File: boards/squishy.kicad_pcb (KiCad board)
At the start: 4 copper layers, 82 x 76.8 mm, 217 parts, among them J1 USB_B_Micro, J2 Conn_02x26_Top_Bottom, J3 Conn_02x05_Odd_Even, U1 128MiB, U10 THVD1451, U11 THVD1451, U12 THVD1451, U13 THVD1451, U14 THVD1451, U15 THVD1451, U16 THVD1451, U17 THVD1451, U18 THVD1451, U19 THVD1451, U2 ICE40HX8K-BG121, U20 THVD1451, U21 TXB0106, U22 TXB0106, U23 TXB0106, U24 TXB0106, U25 TXB0106, U26 TXB0106, U27 FT240XQ, U28 MAX809JTRG, U29 TLV755533PDRVR, U3 THVD1451, U30 TLV73312PQDRVRQ1, U4 THVD1451, U5 THVD1451, U6 THVD1451, U7 THVD1451, U8 THVD1451, U9 THVD1451, X1 ASEM-48MHz

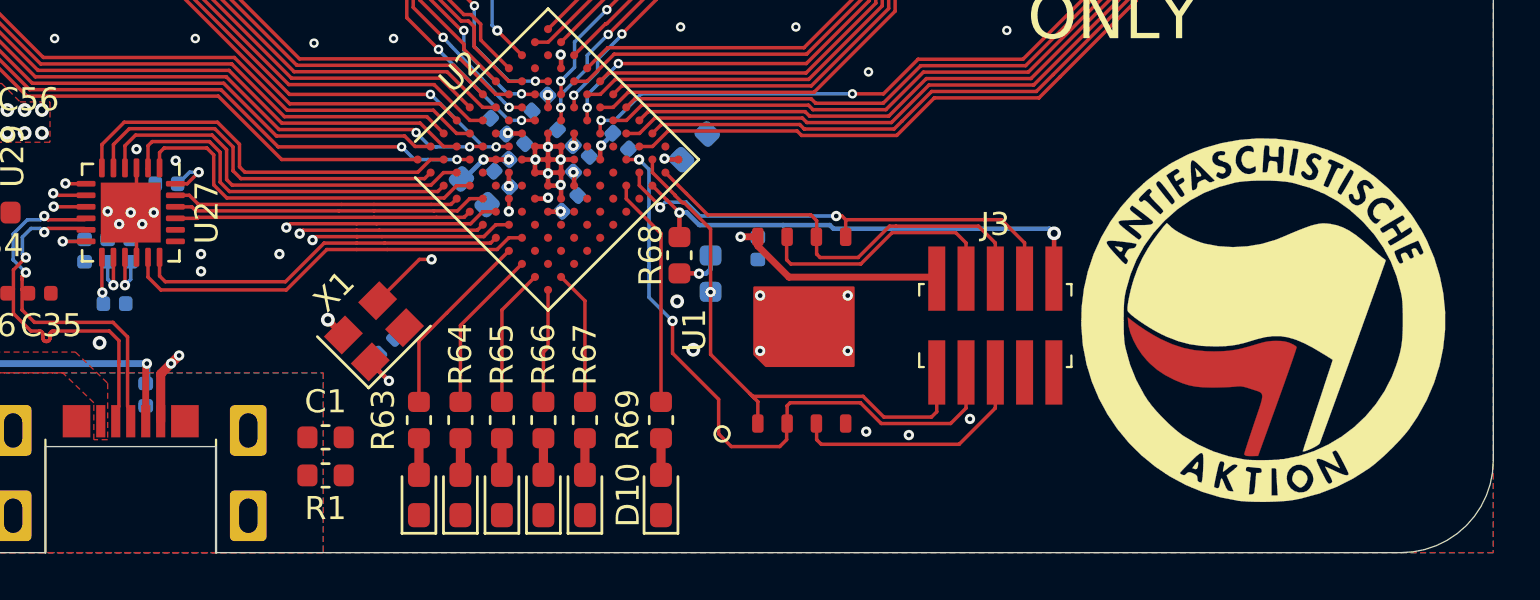
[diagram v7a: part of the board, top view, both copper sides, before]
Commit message: Moved some things around and cached the rev0 of squishy
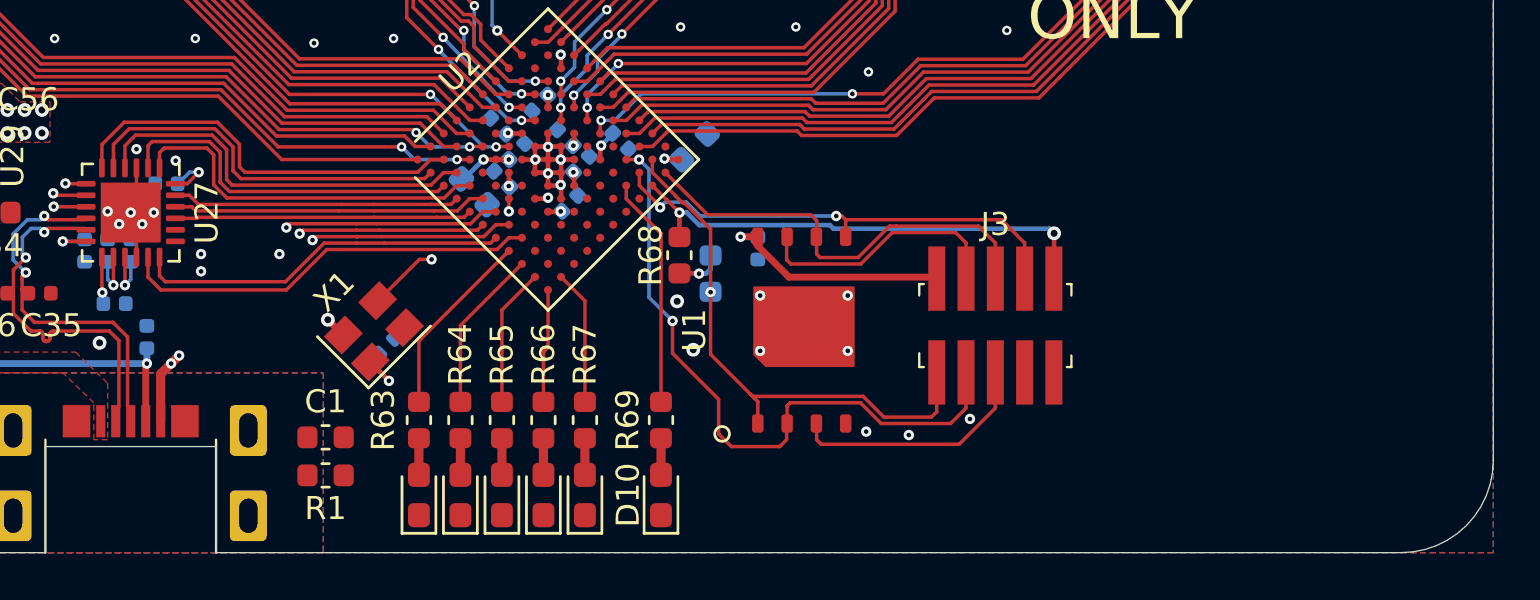
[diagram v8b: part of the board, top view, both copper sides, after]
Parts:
- removed G1: Antifaschistische_Aktion, lethalbit-graphics:Antifaschistische Aktion_600dpi
- moved C3 2.50 mm to (132.6, 111.0), turned to 90 degrees
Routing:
- net +3V3: track 44.8 -> 45.6 mm
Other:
- net class Default removed
